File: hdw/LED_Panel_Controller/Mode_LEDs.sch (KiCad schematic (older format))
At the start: 45 parts, among them U2301 74LVC1G97, U2302 74LVC1G97, U2303 74LVC1G97, U2304 74LVC1G97, U2305 74LVC1G97, U2306 74LVC1G97, U2307 74LVC1G97, U2308 74LVC1G97, U2309 74LVC1G97

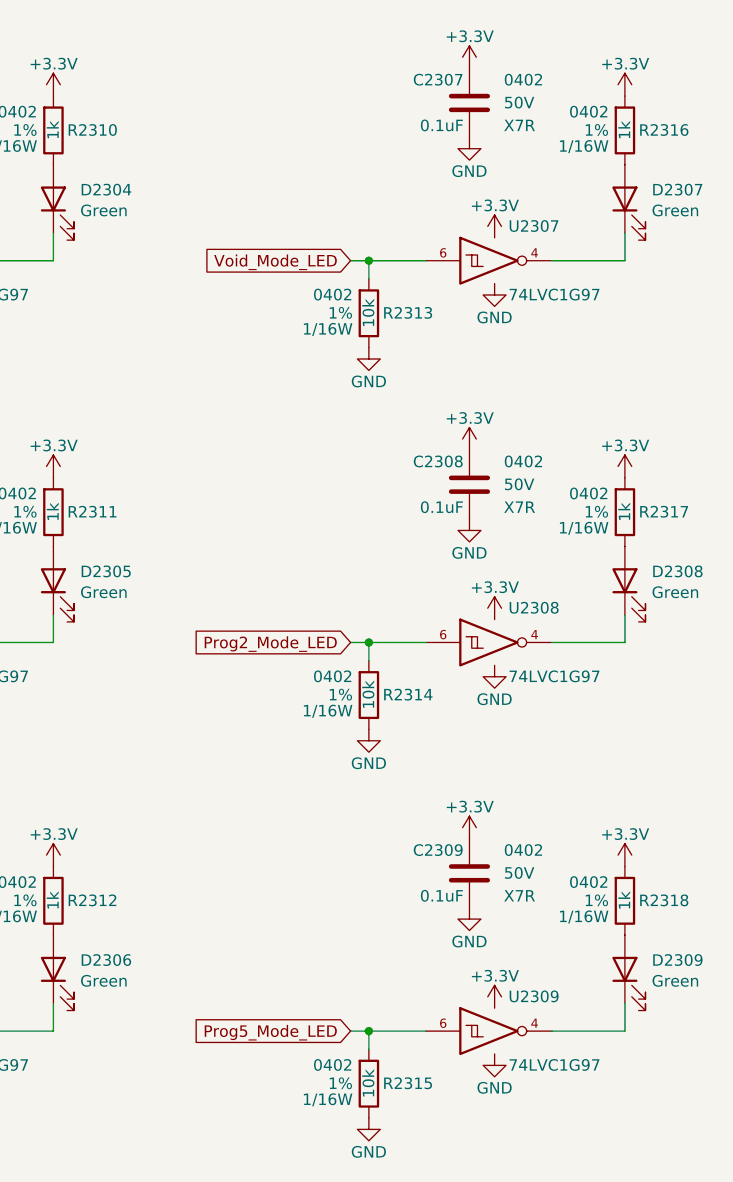
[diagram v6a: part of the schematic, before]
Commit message: ran erc, annotated schematic, added hardstraps to MCU
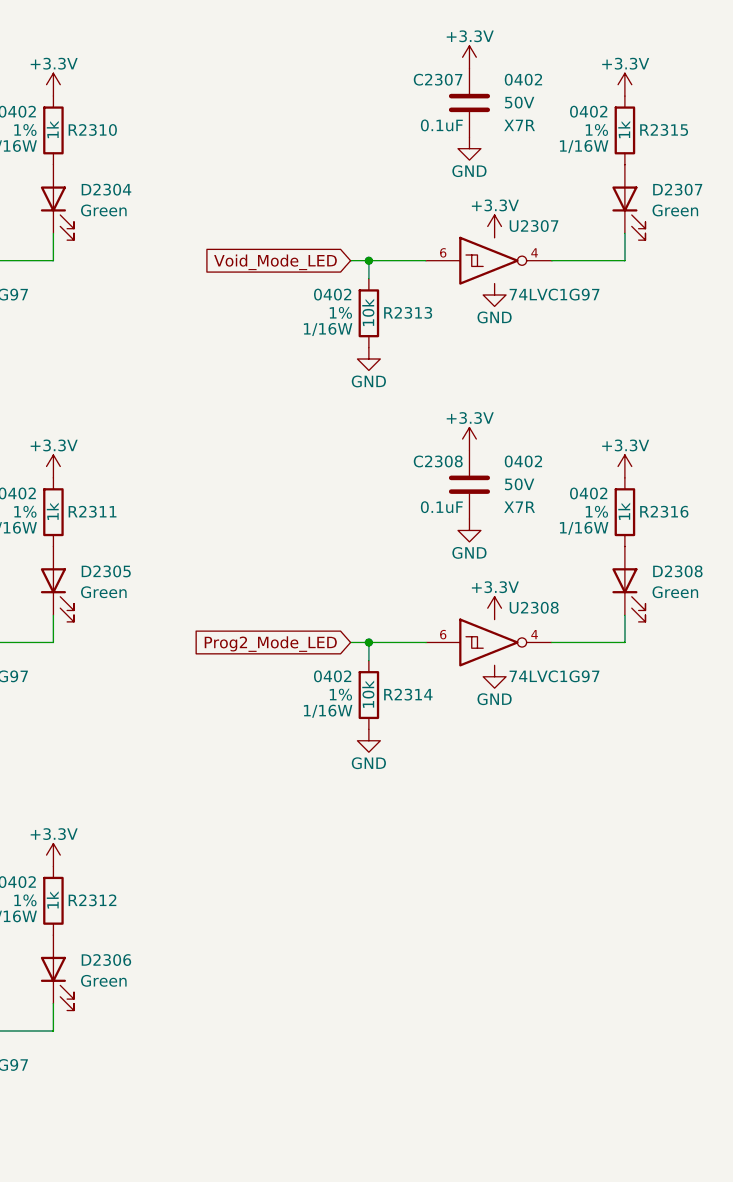
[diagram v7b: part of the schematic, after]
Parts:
- removed C2309: 0.1uF, Capacitors_SMD:C_0402, symbol Custom_Library:C_Custom
- removed D2309: Green, LEDs:LED_0402, symbol Device:LED
- removed R2315: 10k, Resistors_SMD:R_0402, symbol Custom_Library:R_Custom
- removed R2318: 1k, Resistors_SMD:R_0402, symbol Custom_Library:R_Custom
- removed U2309: 74LVC1G97, Package_TO_SOT_SMD:SOT-363_SC-70-6, symbol Custom_Library:74LVC1G97_Power_NOT
- renumbered R2316 to R2315, R2317 to R2316
